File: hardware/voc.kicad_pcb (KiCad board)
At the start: 2 copper layers, 15 x 25 mm, 24 parts, among them P101 CON-SENSOR2, P102 DEBUG, P103 BOOT, U1 BME680, U101 XMC1100-16, U103 DRILL, U104 DRILL, U105 DRILL, U106 DRILL

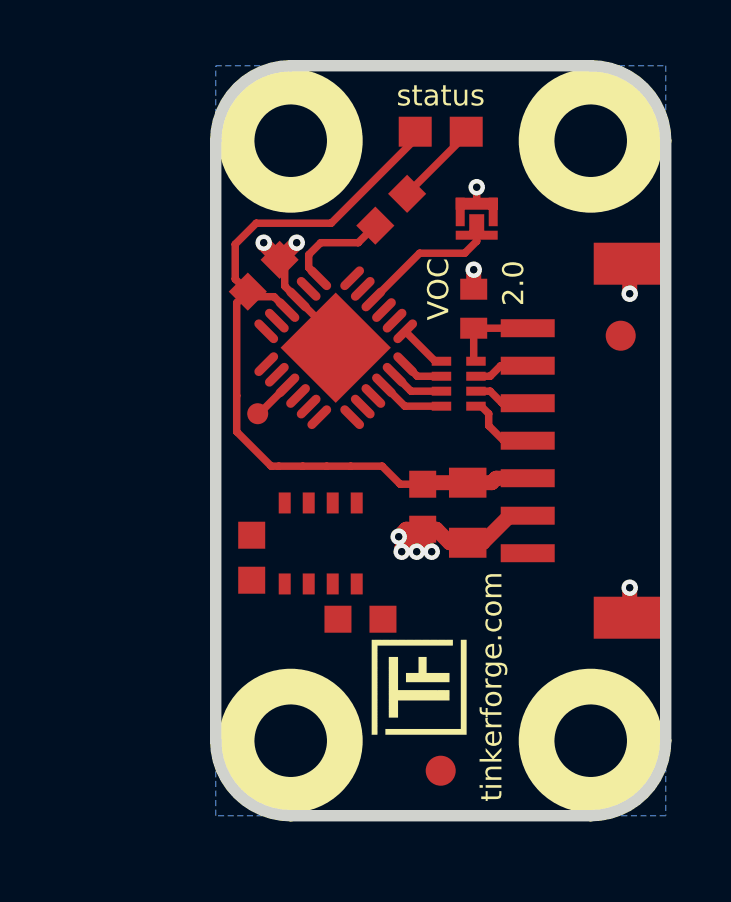
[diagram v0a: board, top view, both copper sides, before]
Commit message: Add routing for BME680
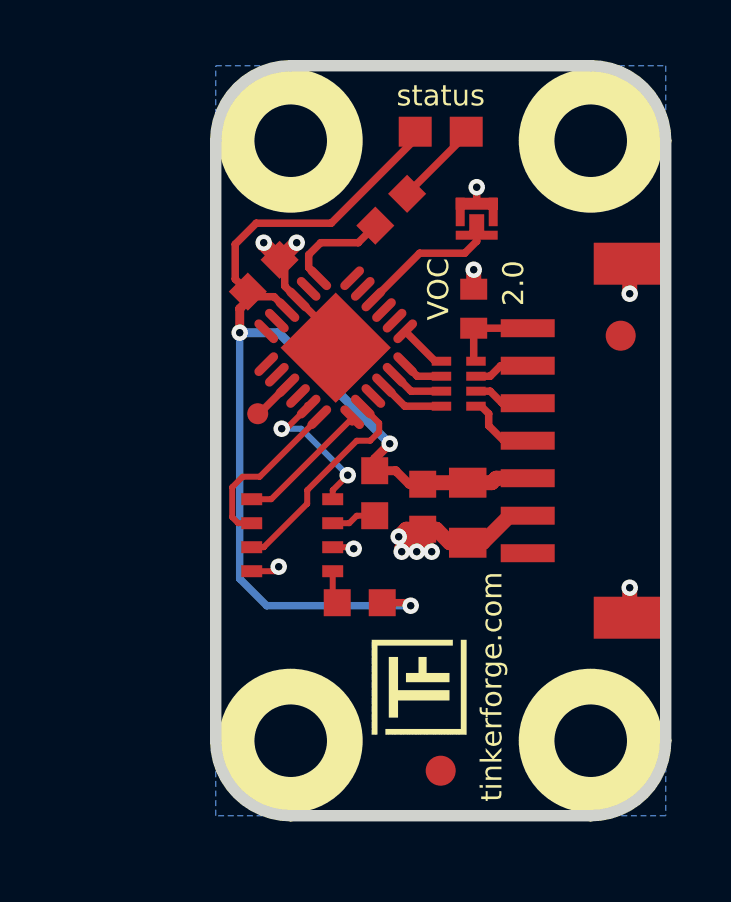
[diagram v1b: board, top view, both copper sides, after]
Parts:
- moved C1 4.23 mm to (145.4, 142.8), turned to 270 degrees
- moved C105 3.90 mm to (144.9, 146.4), turned to 180 degrees
- moved U1 0.99 mm to (142.7, 144.2), turned to 90 degrees
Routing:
- net VCC: track 27.2 -> 40.8 mm, vias 0 -> 3
- net M-CS: track 0.00 -> 7.17 mm
- net M-MOSI: track 0.00 -> 5.45 mm
- net M-MISO: track 0.00 -> 5.20 mm, vias 0 -> 2
- net M-CLK: track 0.00 -> 4.89 mm
- net GND: track 21.3 -> 23.0 mm, vias 10 -> 12
- net Net-(C1-Pad2): track 0.00 -> 1.50 mm
- net Net-(C105-Pad2): track 0.00 -> 1.11 mm

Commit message: Change XMC1100 to XMC1400 footprint
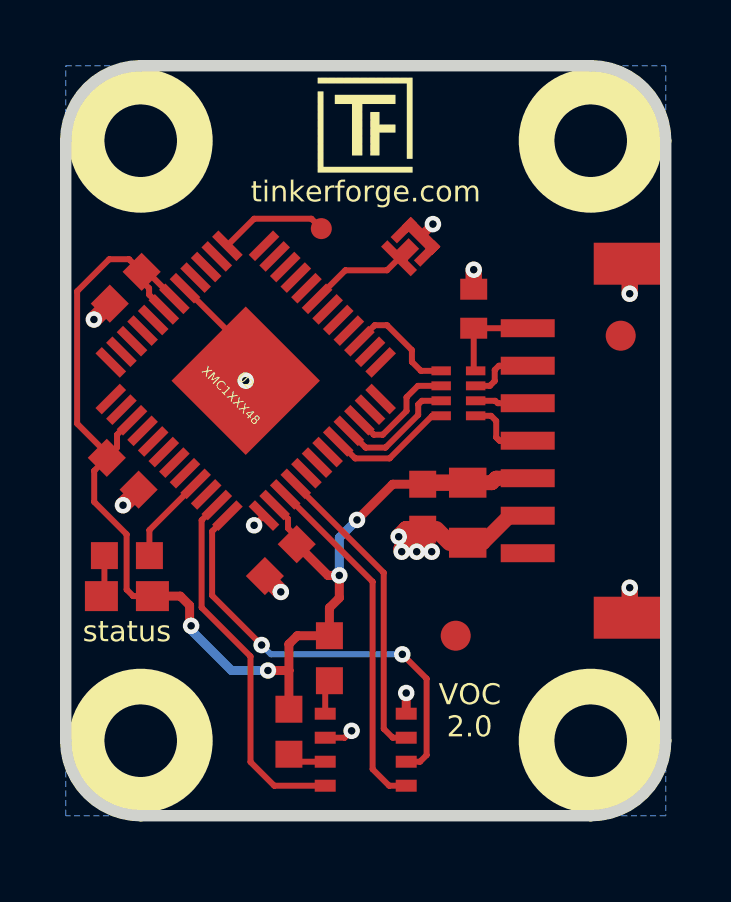
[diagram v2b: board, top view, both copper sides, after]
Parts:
- removed U101: XMC1100-16, kicad-libraries:QFN24-4x4mm-0.5mm
- added C2: 100nF, C0603F, F.Cu at (137.0, 142.1)
- added C3: 100nF, C0603F, F.Cu at (137.1, 135.9)
- added U2: XMC1XXX48, kicad-libraries:QFN48-EP2, F.Cu at (141.1, 139.0)
- moved G*** 22.0 mm to (143.5, 128.9), turned to 0 degrees
- moved D101 18.7 mm to (137.1, 146.2), turned to 180 degrees
- moved R101 14.5 mm to (137.1, 144.8), turned to 180 degrees
- moved VAL 11.0 mm to (138.2, 141.0), turned to 180 degrees
- moved C104 9.50 mm to (142.3, 145.0), turned to 225 degrees
- moved C1 8.45 mm to (142.5, 150.7)
- moved U1 7.56 mm to (145.1, 151.3), turned to 270 degrees
- moved G*** 6.77 mm to (151.2, 141.0), turned to 180 degrees
- moved P102 6.52 mm to (143.6, 133.9)
- moved U105 5.00 mm to (137.6, 131.0)
- moved U106 5.00 mm to (137.6, 151.0)
- moved Fiducial_Mark 4.53 mm to (148.1, 147.5)
- moved G*** 2.76 mm to (144.8, 141.0), turned to 180 degrees
- moved P103 2.39 mm to (146.6, 134.5), turned to 225 degrees
- moved C105 2.11 mm to (143.9, 148.2), turned to 270 degrees
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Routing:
- net M-MOSI: track 5.45 -> 14.5 mm, vias 0 -> 2
- net M-MISO: track 5.20 -> 12.3 mm, vias 2 -> 0
- net M-CLK: track 4.89 -> 11.7 mm
- net M-CS: track 7.17 -> 10.3 mm
- net S-MOSI: track 1.38 -> 3.87 mm
- net S-CLK: track 1.79 -> 4.16 mm
- net Net-(P102-Pad1): track 1.38 -> 3.65 mm
- net S-MISO: track 1.62 -> 3.82 mm
- net VCC: track 40.8 -> 43.0 mm, vias 3 -> 4
- net S-CS: track 2.20 -> 4.25 mm
- net GND: track 23.0 -> 21.2 mm, vias 12 -> 15
- net Net-(D101-Pad2): track 3.03 -> 1.39 mm
- net Net-(P101-Pad6): track 1.87 -> 2.76 mm
- net Net-(P103-Pad2): track 4.85 -> 4.10 mm
- net Net-(R101-Pad1): track 3.55 -> 3.03 mm
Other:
- board size 15 x 25 mm -> 20 x 25 mm

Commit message: Fix version
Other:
- board text added: "1.0"
- board text removed: "2.0"
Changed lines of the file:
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@@
     (links 48)
     (no_connects 0)
-    (area 134.909499 128.309499 155.290501 153.690501)
+    (area 134.244999 127.644999 275.56786 157.715)
     (thickness 1.6)
     (drawings 13)
@@
     (effects (font (size 0.8 0.8) (thickness 0.15)))
   )
-  (gr_text 2.0 (at 148.56 150.53) (layer F.SilkS)
+  (gr_text 1.0 (at 148.56 150.53) (layer F.SilkS)
     (effects (font (size 0.7 0.7) (thickness 0.15)))
   )
